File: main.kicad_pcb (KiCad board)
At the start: 4 copper layers, 100 x 100 mm, 72 parts, among them J101 Conn_Coaxial, J201 Conn_ARM_JTAG_SWD_10, J202 Conn_02x10_Row_Letter_First, Q501 2N7002, Q701 BC847BS, U101 SA818V, U201 STM32U575CITx, U202 CAT24C32, U203 TLV73333PQDBVRQ1, U204 USBLC6-2SC6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

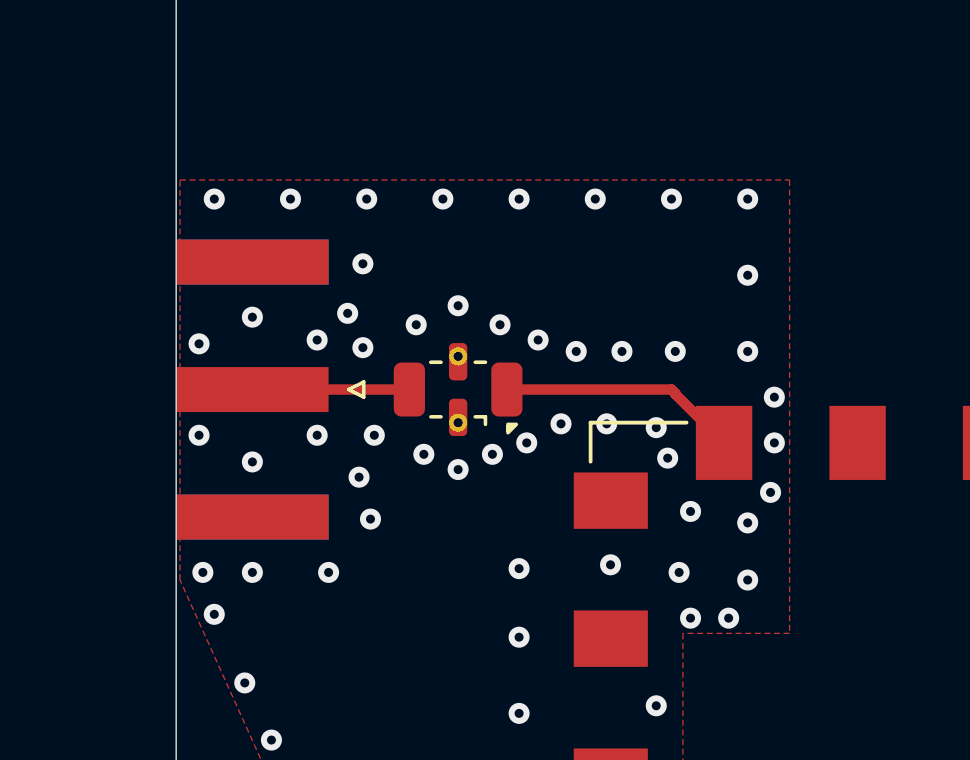
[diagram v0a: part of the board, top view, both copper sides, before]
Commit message: fix pcb gnd
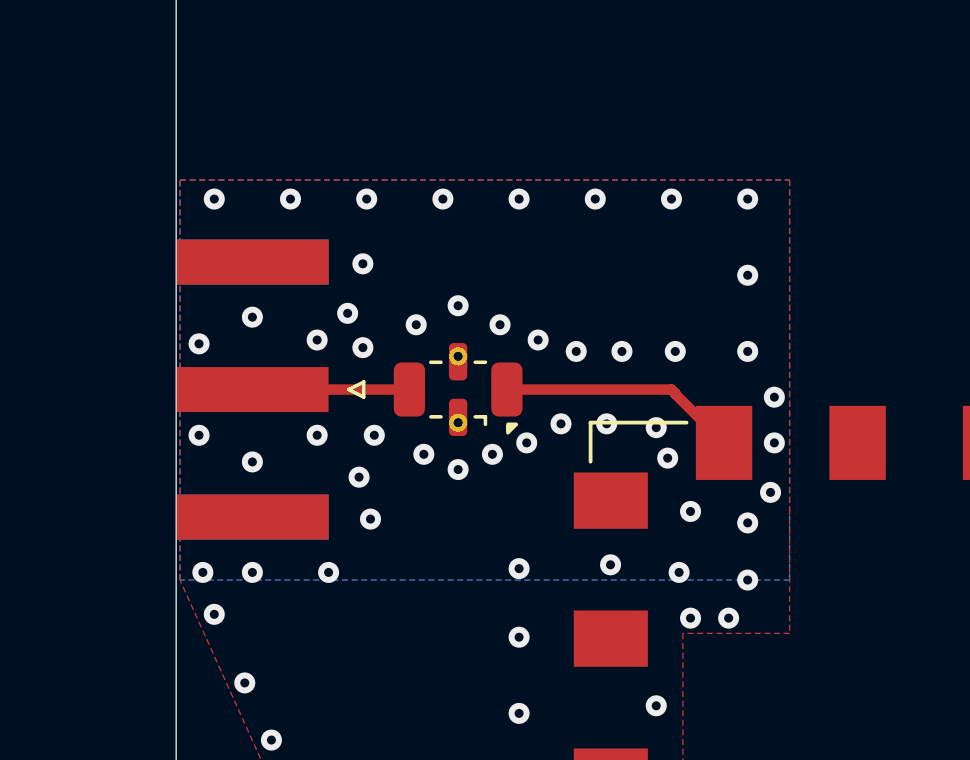
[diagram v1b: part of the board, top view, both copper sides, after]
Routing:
- added copper zone on B.Cu, net GND
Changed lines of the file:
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@@
+	)
+	(zone
+		(net 3)
+		(net_name "+5V")
+		(layer "F.Cu")
+		(hatch edge 0.5)
+		(priority 5)
+		(connect_pads
+			(clearance 0.25)
+		)
+		(min_thickness 0.25)
+		(filled_areas_thickness no)
+		(fill yes
+			(thermal_gap 0.5)
+			(thermal_bridge_width 0.5)
+		)
+		(polygon
+			(pts
+				(xy 192.659 81.102) (xy 188.214 81.102) (xy 187.579 80.975) (xy 181.102 80.975) (xy 181.102 82.245)
+				(xy 182.88 84.15) (xy 185.547 84.15) (xy 187.833 86.055) (xy 192.659 86.055)
+			)
+		)
 	)
 	(zone
@@
 				(xy 114.808 92.532) (xy 109.982 92.532) (xy 109.982 99.009) (xy 110.236 99.644) (xy 110.236 104.724)
 				(xy 107.442 104.724) (xy 98.044 83.896)
-			)
-		)
-	)
-	(zone
-		(net 3)
-		(net_name "+5V")
-		(layer "F.Cu")
-		(hatch edge 0.5)
-		(priority 5)
-		(connect_pads
-			(clearance 0.25)
-		)
-		(min_thickness 0.25)
-		(filled_areas_thickness no)
-		(fill yes
-			(thermal_gap 0.5)
-			(thermal_bridge_width 0.5)
-		)
-		(polygon
-			(pts
-				(xy 192.659 81.102) (xy 188.214 81.102) (xy 187.579 80.975) (xy 181.102 80.975) (xy 181.102 82.245)
-				(xy 182.88 84.15) (xy 185.547 84.15) (xy 187.833 86.055) (xy 192.659 86.055)
 			)
 		)
@@
 			)
 		)
+	)
+	(zone
+		(net 1)
+		(net_name "GND")
+		(layer "B.Cu")
+		(hatch edge 0.5)
+		(priority 6)
+		(connect_pads
+			(clearance 0.25)
+		)
+		(min_thickness 0.25)
+		(filled_areas_thickness no)
+		(fill yes
+			(thermal_gap 0.5)
+			(thermal_bridge_width 0.5)
+		)
+		(polygon
+			(pts
+				(xy 98.044 70.561) (xy 118.364 70.561) (xy 118.364 83.896) (xy 98.044 83.896)
+			)
+		)

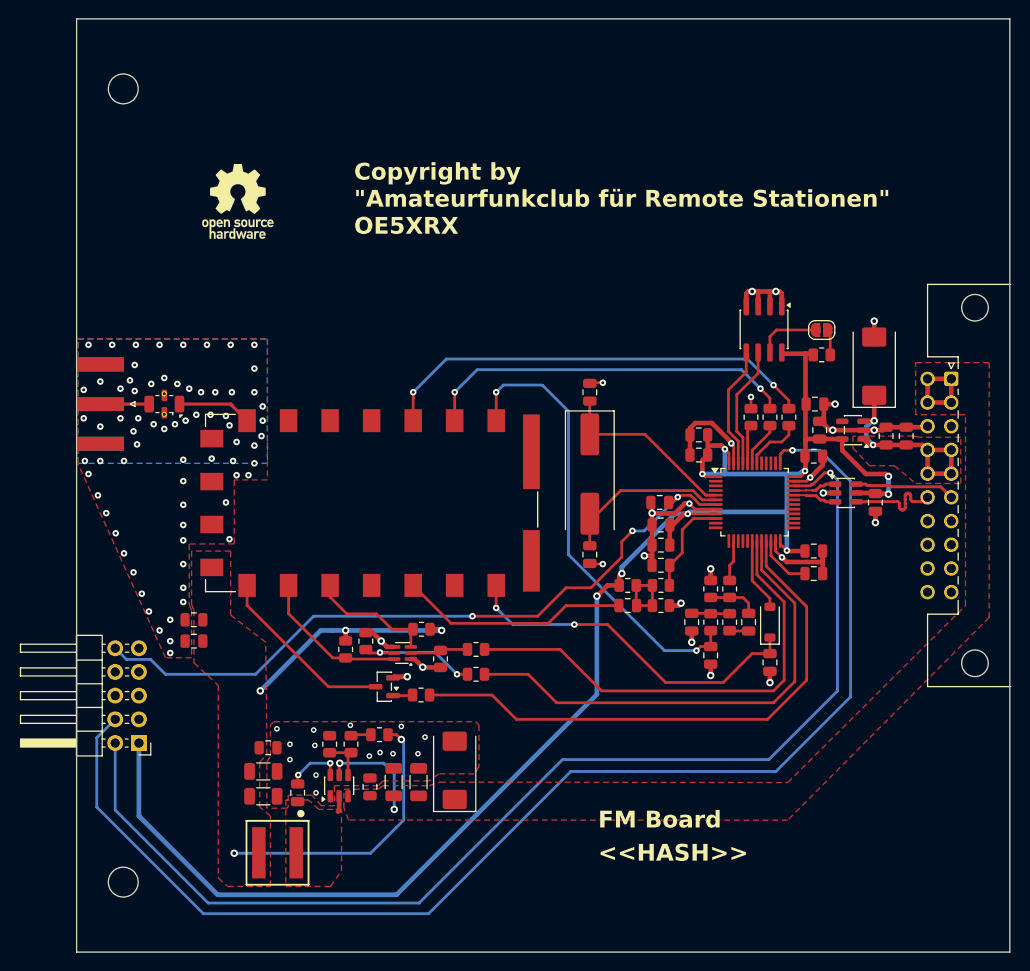
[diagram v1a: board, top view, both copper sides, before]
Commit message: Fix transistor symbol visibility and update polyline coordinates in schematic
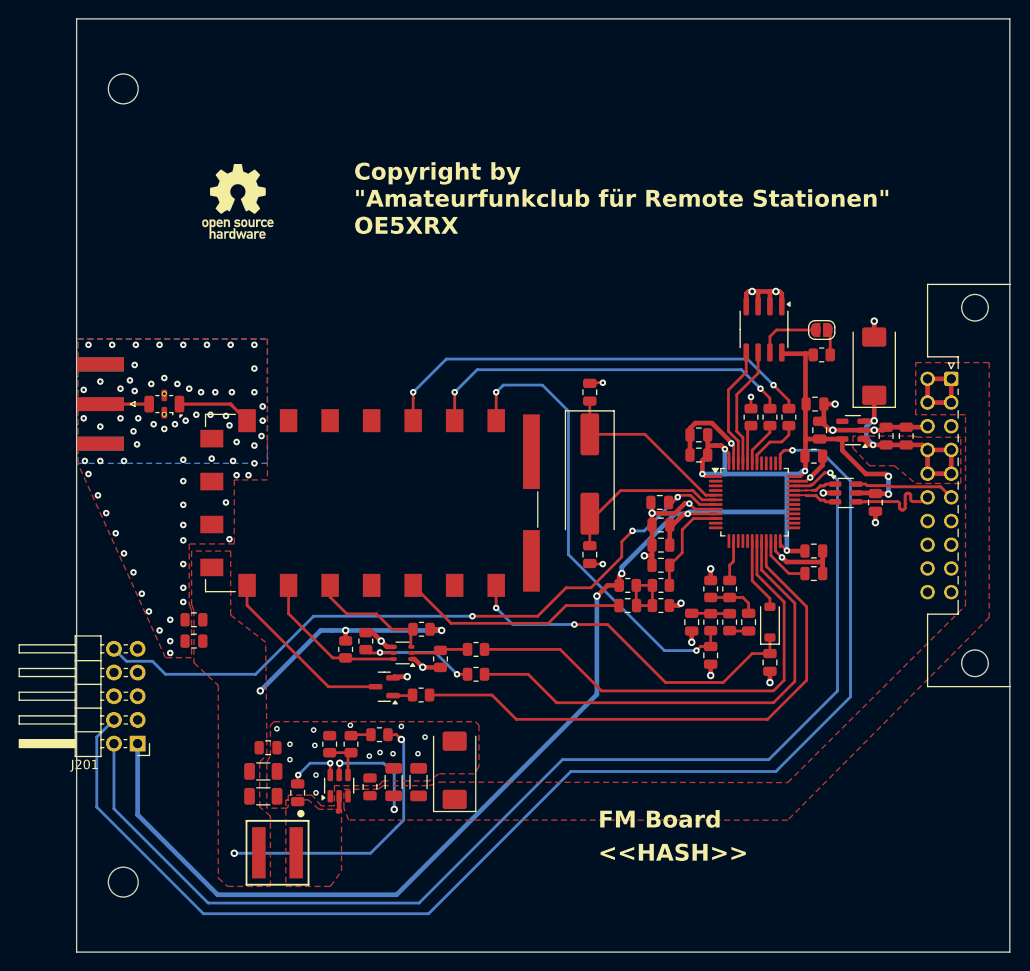
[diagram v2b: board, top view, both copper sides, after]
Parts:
- moved J201 0.15 mm to (104.5, 113.9)
